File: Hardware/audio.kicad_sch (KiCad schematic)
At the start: 35 parts, among them J13 ANT_BNC, J14 ANT_BNC, J15 Audio IN, Q3 MMBT2222A, U10 Si4732, U9 LM358, X1 Q13FC1350000400

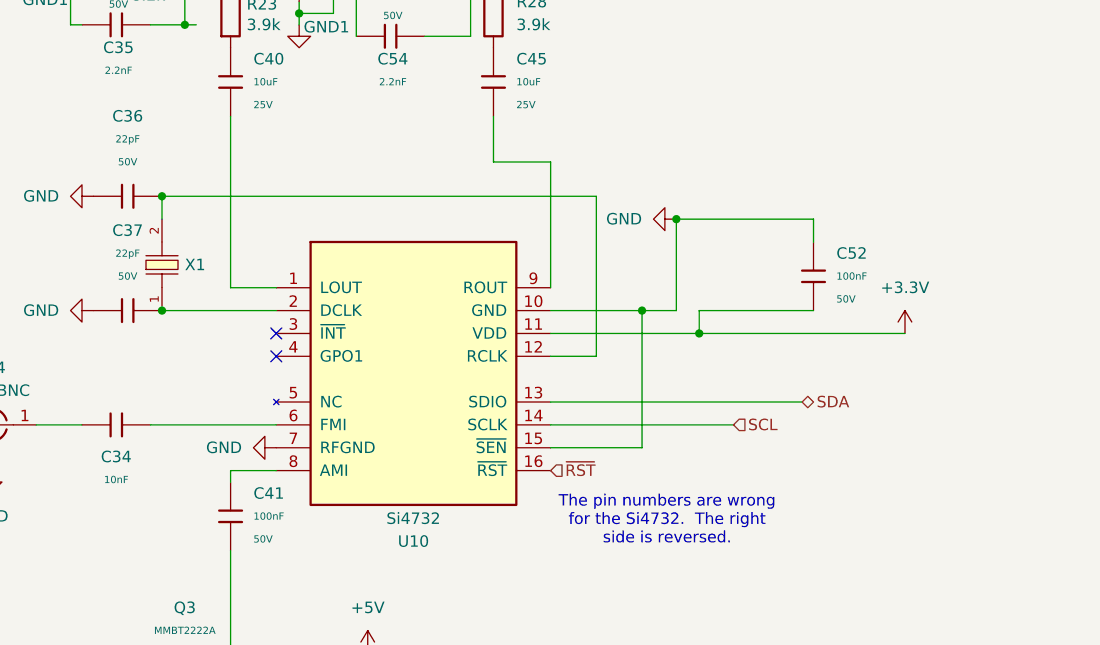
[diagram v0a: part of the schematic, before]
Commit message: Fixed pins on Si4732 and created a README with instructions on fixing the YD-RP2040 pinout
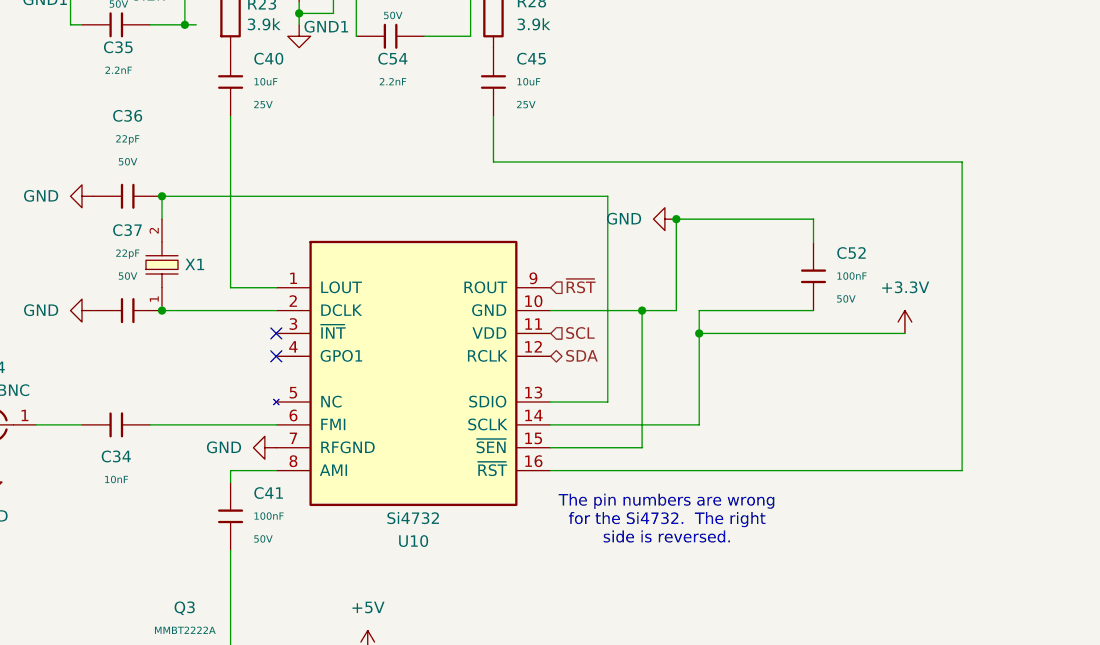
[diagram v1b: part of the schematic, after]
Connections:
- net +3.3V: now also U10.14 (SCLK); no longer U10.11 (VDD)
- net SCL: now also U10.11 (VDD); no longer U10.14 (SCLK)
- net SDA: now also U10.12 (RCLK); no longer U10.13 (SDIO)
- net ~{RST}: now also U10.9 (ROUT); no longer U10.16 (~{RST})
- net at C36.2, X1.2: now also U10.13 (SDIO); no longer U10.12 (RCLK)
- net at C45.2: now also U10.16 (~{RST}); no longer U10.9 (ROUT)
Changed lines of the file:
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@@
+	)
+	(junction
+		(at 63.5 110.49)
+		(diameter 0)
+		(color 0 0 0 0)
+	)
+	(junction
+		(at 68.58 50.8)
+		(diameter 0)
+		(color 0 0 0 0)
+	)
+	(junction
+		(at 86.36 68.58)
+		(diameter 0)
+		(color 0 0 0 0)
 	)
 	(junction
 		(at 123.19 113.03)
-		(diameter 0)
-		(color 0 0 0 0)
-	)
-	(junction
-		(at 63.5 110.49)
-		(diameter 0)
-		(color 0 0 0 0)
-	)
-	(junction
-		(at 68.58 50.8)
-		(diameter 0)
-		(color 0 0 0 0)
-	)
-	(junction
-		(at 86.36 68.58)
 		(diameter 0)
 		(color 0 0 0 0)
@@
 	(wire
 		(pts
+			(xy 106.68 123.19) (xy 123.19 123.19)
+		)
+		(stroke
+			(width 0)
+			(type default)
+		)
+	)
+	(wire
+		(pts
 			(xy 120.65 100.33) (xy 120.65 110.49)
 		)
@@
 	(wire
 		(pts
-			(xy 106.68 93.98) (xy 100.33 93.98)
+			(xy 100.33 93.98) (xy 152.4 93.98)
 		)
 		(stroke
@@
 	(wire
 		(pts
-			(xy 106.68 123.19) (xy 127 123.19)
-		)
-		(stroke
-			(width 0)
-			(type default)
-		)
-	)
-	(wire
-		(pts
 			(xy 86.36 148.59) (xy 86.36 149.86)
 		)
@@
 	(wire
 		(pts
-			(xy 106.68 115.57) (xy 111.76 115.57)
-		)
-		(stroke
-			(width 0)
-			(type default)
-		)
-	)
-	(wire
-		(pts
 			(xy 62.23 123.19) (xy 76.2 123.19)
 		)
@@
 	(wire
 		(pts
+			(xy 113.03 97.79) (xy 113.03 120.65)
+		)
+		(stroke
+			(width 0)
+			(type default)
+		)
+	)
+	(wire
+		(pts
 			(xy 123.19 110.49) (xy 135.89 110.49)
 		)
@@
 	(wire
 		(pts
-			(xy 106.68 113.03) (xy 123.19 113.03)
+			(xy 106.68 120.65) (xy 113.03 120.65)
 		)
 		(stroke
@@
 	(wire
 		(pts
-			(xy 111.76 115.57) (xy 111.76 97.79)
-		)
-		(stroke
-			(width 0)
-			(type default)
-		)
-	)
-	(wire
-		(pts
 			(xy 53.34 78.74) (xy 53.34 73.66)
 		)
@@
 	(wire
 		(pts
+			(xy 123.19 123.19) (xy 123.19 113.03)
+		)
+		(stroke
+			(width 0)
+			(type default)
+		)
+	)
+	(wire
+		(pts
 			(xy 106.68 110.49) (xy 116.84 110.49)
 		)
@@
 	(wire
 		(pts
-			(xy 106.68 107.95) (xy 106.68 93.98)
-		)
-		(stroke
-			(width 0)
-			(type default)
-		)
-	)
-	(wire
-		(pts
 			(xy 121.92 69.85) (xy 130.81 69.85)
 		)
@@
 	(wire
 		(pts
+			(xy 152.4 93.98) (xy 152.4 128.27)
+		)
+		(stroke
+			(width 0)
+			(type default)
+		)
+	)
+	(wire
+		(pts
 			(xy 100.33 66.04) (xy 100.33 73.66)
 		)
@@
 	(wire
 		(pts
+			(xy 106.68 128.27) (xy 152.4 128.27)
+		)
+		(stroke
+			(width 0)
+			(type default)
+		)
+	)
+	(wire
+		(pts
 			(xy 62.23 78.74) (xy 66.04 78.74)
 		)
@@
 	(wire
 		(pts
-			(xy 111.76 97.79) (xy 63.5 97.79)
+			(xy 113.03 97.79) (xy 63.5 97.79)
 		)
 		(stroke
@@
 	(wire
 		(pts
-			(xy 106.68 120.65) (xy 134.62 120.65)
-		)
-		(stroke
-			(width 0)
-			(type default)
-		)
-	)
-	(wire
-		(pts
 			(xy 86.36 36.83) (xy 97.79 36.83)
 		)
@@
 		)
 	)
-	(hierarchical_label "SDA"
-		(shape bidirectional)
-		(at 134.62 120.65 0)
+	(hierarchical_label "~{RST}"
+		(shape input)
+		(at 106.68 107.95 0)
 		(effects
 			(font
@@
 		)
 	)
-	(hierarchical_label "~{RST}"
+	(hierarchical_label "SCL"
 		(shape input)
-		(at 106.68 128.27 0)
+		(at 106.68 113.03 0)
 		(effects
 			(font
@@
 		)
 	)
-	(hierarchical_label "SCL"
-		(shape input)
-		(at 127 123.19 0)
+	(hierarchical_label "SDA"
+		(shape bidirectional)
+		(at 106.68 115.57 0)
 		(effects
 			(font
